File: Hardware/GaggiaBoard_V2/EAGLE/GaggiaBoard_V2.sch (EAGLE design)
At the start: 127 parts, among them IC1 LD117AS33TR, IC2 LD117AS33TR, J10 PIN262409-1, J11 PIN262409-1, J12 PIN262409-1, J13 PIN262409-1, J14 PIN262409-1, J15 PIN262409-1, J16 PIN262409-1, J17 PIN262409-1, J18 PIN262409-1, J19 PIN262409-1, J2 Vertical Qwiic Connector, J20 PIN262409-1, J21 PIN262409-1, J22 PIN262409-1, J23 PIN262409-1, J24 5033981892, J3 Vertical Qwiic Connector, J4 1X2-3.5MM, J5 1X2-3.5MM, K1 RELAY-SPDT-JZC-11F, K2 RELAY-SPDT-JZC-11F, K3 RELAY-SPDT-JZC-11F, Q1 600mA/40V, Q10 600mA/40V, Q11 MOSFET_PCH_DUAL-DMP2240UDM, Q2 600mA/40V, Q3 600mA/40V, Q4 600mA/40V, Q5 600mA/40V, Q6 600mA/40V, Q8 600mA/40V, Q9 600mA/40V, U1 BLACKPILL, U2 MAX31855K, U3 MAX31855K, U5 TXS0102

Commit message: V2 initial state
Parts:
- removed C14: 0.1uF, rcl:C-USC0603
- removed C4: 0.01uF, rcl:C-USC0603
- removed D6: (no value), adafruit:DIODESOD-123
- removed FB3, FB4: 470Ω, SparkFun-Coils:FERRITE_BEAD-0603-470Ω-100MHZ-1A-200MILIΩ
- removed J10, J21, J22, J23: PIN262409-1, con-faston:PIN262409-1
- removed LED4: (no value), adafruit:LEDCHIPLED_1206
- removed PSU2: IRM-10-5, discrete:IRM-10-5
- removed R29: 10K, rcl:R-US_R0603
- removed R30: 1K, rcl:R-US_R0603
- removed SPK1: SMT-0540-S-R, adafruit:SMT-0540-S-R
- removed U3: MAX31855K, SparkFun-IC-Conversion:MAX31855K
- added C15: 0.1uF, rcl:C-USC0603
- added H1: STANDOFF_ELECTRICAL, SparkFun-Hardware:STANDOFF_ELECTRICAL
- added SP1: SPEAKER/AL60P, adafruit:SPEAKER/AL60P
- F1: device special:FUSE2P -> special:FUSE
- J27: device SparkFun-Connectors:CONN_05NO_SILK -> SparkFun-Connectors:CONN_06NO_SILK_FEMALE_PTH
- J4: value 1X2-3.5MM -> (none); device adafruit:1X2-3.5MM -> SparkFun-Connectors:CONN_03SCREW; LCSC C474892 -> C474893
- J5: value 1X2-3.5MM -> 2PIN; device adafruit:1X2-3.5MM -> jst_eph:2PIN; LCSC C474892 -> C131337
- J6, J7, J9: value (none) -> 3PIN; device SparkFun-Connectors:CONN_03JST-PTH-VERT -> jst_eph:3PIN
- J8: value (none) -> 5PIN; device SparkFun-Connectors:CONN_05JST-VERT -> jst_eph:5PIN
- PSU1: value SM-PLG06-05 -> IRM-10-5; device discrete:SM-PLG06-05 -> discrete:IRM-10-5; SPICEPREFIX (none) -> E
- R12: value 51 -> 10K; LCSC C114628 -> C98220
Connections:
- net UART6_5V_RX renamed UART2_5V_RX
- net UART6_5V_TX renamed UART2_5V_TX
- removed net N$23: FB3.1, J5.1
- removed net N$25: C4.1, FB4.2, U3.T-
- removed net N$27: LED4.C, R12.2
- removed net N$31: C4.2, FB3.2, U3.T+
- removed net N$6: FB4.1, J5.2
- removed net PA2: J7.3, U1.PA2
- removed net PB2: J8.5, U1.PB2
- removed net RTS: C14.1, J27.5, R30.2
- removed net SPI2_MISO: U1.PB14, U2.(MI)SO, U3.(MI)SO
- removed net SPI2_NSS: U1.PB12, U2.!CS
- removed net SPI2_NSS2: U1.PB9, U3.!CS
- removed net SPI2_SCK: U1.PB13, U2.SCK, U3.SCK
- removed net UART6_RX: Q7G$2.S, R18.1, SJ2.1, U1.PA12
- removed net UART6_TX: Q7G$1.S, R19.1, SJ1.1, U1.PA11
- new net BOOT1: J27.6, U1.PB2
- new net PA15: R33.2, U1.PA15
- new net PB12: R6.1, U1.PB12
- new net PB13: R7.1, U1.PB13
- new net PB14: R28.1, U1.PB14
- new net PB15: J5.2, U1.PB15
- new net PB9: J8.5, U1.PB9
- new net UART2_RX: Q7G$2.S, R18.1, SJ2.1, U1.PA3
- new net UART2_TX: Q7G$1.S, R19.1, SJ1.1, U1.PA2
- net 3V3: now also C15.1; no longer C8.1, D1.C, D6.C, LED4.A, R27.2, R29.2, SPK1.-, U3.VCC
- net 3WAY: now also J16.1, K3.NO; no longer J11.1, K1.NO
- net 5V: now also C8.1, D1.C, R12.2, R27.2, SP1.-; no longer PSU2.VO+
- net AC_N: now also J15.1, J18.1, J19.1; no longer J10.1, J16.1, J21.1, J22.1, PSU2.AC_N
- net AC_P: now also F1.2, J13.1; no longer F1.2A, J15.1, J19.1, PSU2.AC_L
- net GND: now also C15.2, H1.P$1, J4.3, J5.1; no longer PSU2.VO-, R12.1, R30.1, U3.GND
- net HEATER_1: no longer J13.1
- net HEATER_2: now also J11.1, K1.NO; no longer J17.1, J18.1, K3.NO
- net I2C1_SCL: now also U5.A1
- net I2C1_SDA: now also U5.A2
- net I2C2_SCL: no longer U5.A1
- net I2C2_SDA: no longer U5.A2
- net N$1: now also F1.1, J20.1; no longer F1.1A, J23.1
- net N$3: now also J4.1; no longer J4.2
- net N$30: now also R12.1, SP1.+; no longer SPK1.+
- net N$4: now also J4.2; no longer J4.1
- net N$41: now also J9.3; no longer J9.2
- net N$42: now also J9.2; no longer J9.3
- net NRST: now also J27.5; no longer C14.2, D6.A, R29.1
- net PA1: now also R1.1; no longer J7.2
- net PA6: now also U2.!CS; no longer R34.2
- net PA8: now also R34.2; no longer R33.2
- net PB1: no longer J8.1
- net PB5: no longer R28.1
- net PB8: now also J8.1; no longer R1.1
- net PC14: now also J7.3; no longer R7.1
- net PC15: now also J7.2; no longer R6.1
- net PUMP_P: now also J17.1; no longer J20.1
- net SPI1_MISO: now also U2.(MI)SO
- net SPI1_SCK: now also U2.SCK
- net UART1_RX: now also J27.2; no longer J27.3
- net UART1_TX: now also J27.3; no longer J27.2
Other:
- moved on the sheet: C10, C11, C13, C3, C8, C9, D2, D3, D4, FB1, FB2, J11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

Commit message: part list fix
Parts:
- IC1, IC2: LCSC C152529 -> C26537
- LED1, LED2, LED3: LCSC C375534 -> C125086
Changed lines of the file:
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@@
 </part>
 <part name="LED1" library="adafruit" library_urn="urn:adsk.eagle:library:420" deviceset="LED" device="CHIPLED_1206" package3d_urn="urn:adsk.eagle:package:6240560/1" override_package3d_urn="urn:adsk.eagle:package:36462256/4" override_package_urn="urn:adsk.eagle:footprint:6239914/1">
-<attribute name="LCSC" value="C375534"/>
+<attribute name="LCSC" value="C125086"/>
 </part>
 <part name="LED2" library="adafruit" library_urn="urn:adsk.eagle:library:420" deviceset="LED" device="CHIPLED_1206" package3d_urn="urn:adsk.eagle:package:6240560/1" override_package3d_urn="urn:adsk.eagle:package:36462272/2" override_package_urn="urn:adsk.eagle:footprint:6239914/1">
-<attribute name="LCSC" value="C375534"/>
+<attribute name="LCSC" value="C125086"/>
 </part>
 <part name="LED3" library="adafruit" library_urn="urn:adsk.eagle:library:420" deviceset="LED" device="CHIPLED_1206" package3d_urn="urn:adsk.eagle:package:6240560/1" override_package3d_urn="urn:adsk.eagle:package:36462279/2" override_package_urn="urn:adsk.eagle:footprint:6239914/1">
-<attribute name="LCSC" value="C375534"/>
+<attribute name="LCSC" value="C125086"/>
 </part>
 <part name="R10" library="rcl" library_urn="urn:adsk.eagle:library:334" deviceset="R-US_" device="R0603" package3d_urn="urn:adsk.eagle:package:23555/3" value="120">
@@
 </part>
 <part name="IC1" library="v-reg" library_urn="urn:adsk.eagle:library:409" deviceset="LD117A?*" device="S" package3d_urn="urn:adsk.eagle:package:30370/1" override_package3d_urn="urn:adsk.eagle:package:36461295/2" override_package_urn="urn:adsk.eagle:footprint:30315/1" technology="33TR" value="LD117AS33TR">
-<attribute name="LCSC" value="C152529"/>
+<attribute name="LCSC" value="C26537"/>
 </part>
 <part name="SUPPLY9" library="Power_Symbols" library_urn="urn:adsk.eagle:library:16502351" deviceset="GND-BAR" device="" value="GND"/>
@@
 </part>
 <part name="IC2" library="v-reg" library_urn="urn:adsk.eagle:library:409" deviceset="LD117A?*" device="S" package3d_urn="urn:adsk.eagle:package:30370/1" override_package3d_urn="urn:adsk.eagle:package:36461293/2" override_package_urn="urn:adsk.eagle:footprint:30315/1" technology="33TR" value="LD117AS33TR">
-<attribute name="LCSC" value="C152529"/>
+<attribute name="LCSC" value="C26537"/>
 </part>
 <part name="SUPPLY13" library="Power_Symbols" library_urn="urn:adsk.eagle:library:16502351" deviceset="GND-BAR" device="" value="GND"/>

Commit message: V2.1 update
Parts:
- removed IC2: LD117AS33TR, v-reg:LD117AS33TR
- removed J24: 5033981892, discrete:5033981892
- removed Q7: (no value), microbuilder:MOSFET-N_DUAL
- removed R16, R17, R18, R19: 10K, rcl:R-US_R0603
- removed SJ1, SJ2: (no value), microbuilder:SOLDERJUMPER
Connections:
- removed net UART2_5V_RX: J1.2, Q7G$2.D, R16.1, SJ2.2
- removed net UART2_5V_TX: J1.3, Q7G$1.D, R17.1, SJ1.2
- net 3V3: no longer IC2.OUT, J24.VDD, Q7G$1.G, Q7G$2.G, R18.2, R19.2
- net 5V: no longer IC2.IN, R16.2, R17.2
- net GND: no longer IC2.ADJ, J24.VSS
- net SPI1_MISO: no longer J24.DAT0
- net SPI1_MOSI: no longer J24.CMD
- net SPI1_NSS: no longer J24.CD/DAT3
- net SPI1_SCK: no longer J24.CLK
- net UART2_RX: now also J1.2; no longer Q7G$2.S, R18.1, SJ2.1
- net UART2_TX: now also J1.3; no longer Q7G$1.S, R19.1, SJ1.1
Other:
- moved on the sheet: IC1

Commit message: J1 fix
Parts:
- J1: value (none) -> 4PIN; device SparkFun-Connectors:CONN_04POLAR -> jst_exh:4PIN
- PSU1: LCSC (none) -> C2857903
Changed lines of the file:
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@@
 </classes>
 <parts>
-<part name="J1" library="SparkFun-Connectors" deviceset="CONN_04" device="POLAR" override_package3d_urn="urn:adsk.eagle:package:36462044/3" override_package_urn="urn:adsk.eagle:footprint:36462045/1">
-<attribute name="LCSC" value="C144395"/>
-</part>
 <part name="U1" library="discrete" library_urn="urn:adsk.eagle:library:211" deviceset="BLACKPILL" device="" override_package3d_urn="urn:adsk.eagle:package:36462313/2" override_package_urn="urn:adsk.eagle:footprint:36462314/1"/>
 <part name="J2" library="SparkFun-Connectors" deviceset="QWIIC_CONNECTOR" device="" override_package3d_urn="urn:adsk.eagle:package:36462029/2" override_package_urn="urn:adsk.eagle:footprint:36462030/1" value="Vertical Qwiic Connector">
@@
 </part>
 <part name="PSU1" library="discrete" deviceset="IRM-10-5" device="" override_package3d_urn="urn:adsk.eagle:package:36415007/2" override_package_urn="urn:adsk.eagle:footprint:36415008/1" override_locally_modified="yes">
+<attribute name="LCSC" value="C2857903"/>
 <attribute name="SPICEPREFIX" value="E"/>
 </part>
@@
 </spice>
 <attribute name="LCSC" value="C98220"/>
+</part>
+<part name="J1" library="jst_exh" deviceset="4PIN" device="" override_package3d_urn="urn:adsk.eagle:package:37572770/2" override_package_urn="urn:adsk.eagle:footprint:37572771/1">
+<attribute name="LCSC" value="C144395"/>
 </part>
 </parts>
@@
 </plain>
 <instances>
-<instance part="J1" gate="J1" x="10.16" y="170.18" smashed="yes">
-<attribute name="VALUE" x="5.08" y="162.814" size="1.778" layer="96" font="vector"/>
-<attribute name="NAME" x="5.08" y="178.308" size="1.778" layer="95" font="vector"/>
-<attribute name="LCSC" x="10.16" y="170.18" size="1.778" layer="96" display="off"/>
-</instance>
 <instance part="U1" gate="G$1" x="203.2" y="144.78" smashed="yes">
 <attribute name="NAME" x="193.04" y="173.482" size="1.27" layer="94"/>
@@
 <attribute name="VALUE" x="55.88" y="165.735" size="1.778" layer="96" align="center"/>
 </instance>
+<instance part="J1" gate="G$1" x="12.7" y="170.18" smashed="yes" rot="R180">
+<attribute name="NAME" x="12.7" y="180.34" size="1.27" layer="95" rot="R180"/>
+<attribute name="LCSC" x="12.7" y="170.18" size="1.778" layer="96" rot="R180" display="off"/>
+</instance>
 </instances>
 <busses>
@@
 <net name="GND" class="0">
 <segment>
-<pinref part="J1" gate="J1" pin="4"/>
-<wire x1="15.24" y1="175.26" x2="22.86" y2="175.26" width="0.1524" layer="91"/>
-<label x="17.78" y="175.26" size="1.778" layer="95"/>
+<label x="20.32" y="175.26" size="1.778" layer="95"/>
+<wire x1="17.78" y1="175.26" x2="27.94" y2="175.26" width="0.1524" layer="91"/>
+<pinref part="J1" gate="G$1" pin="4"/>
 </segment>
 <segment>
@@
 <net name="5V" class="0">
 <segment>
-<pinref part="J1" gate="J1" pin="1"/>
-<wire x1="15.24" y1="167.64" x2="22.86" y2="167.64" width="0.1524" layer="91"/>
 <label x="20.32" y="167.64" size="1.778" layer="95"/>
+<wire x1="17.78" y1="167.64" x2="27.94" y2="167.64" width="0.1524" layer="91"/>
+<pinref part="J1" gate="G$1" pin="1"/>
 </segment>
 <segment>
@@
 </segment>
 <segment>
-<pinref part="J1" gate="J1" pin="2"/>
-<wire x1="15.24" y1="170.18" x2="22.86" y2="170.18" width="0.1524" layer="91"/>
-<label x="17.78" y="170.18" size="1.778" layer="95"/>
+<label x="20.32" y="170.18" size="1.778" layer="95"/>
+<wire x1="17.78" y1="170.18" x2="27.94" y2="170.18" width="0.1524" layer="91"/>
+<pinref part="J1" gate="G$1" pin="2"/>
 </segment>
 </net>
@@
 </segment>
 <segment>
-<pinref part="J1" gate="J1" pin="3"/>
-<wire x1="15.24" y1="172.72" x2="22.86" y2="172.72" width="0.1524" layer="91"/>
-<label x="17.78" y="172.72" size="1.778" layer="95"/>
+<label x="20.32" y="172.72" size="1.778" layer="95"/>
+<wire x1="17.78" y1="172.72" x2="27.94" y2="172.72" width="0.1524" layer="91"/>
+<pinref part="J1" gate="G$1" pin="3"/>
 </segment>
 </net>
@@
 <attribute name="NAME" x="55.88" y="43.18" size="1.27" layer="95"/>
 <attribute name="VALUE" x="55.88" y="27.94" size="1.27" layer="96"/>
+<attribute name="LCSC" x="63.5" y="35.56" size="1.778" layer="96" display="off"/>
 </instance>
 <instance part="SUPPLY23" gate="G$1" x="78.74" y="27.94" smashed="yes">

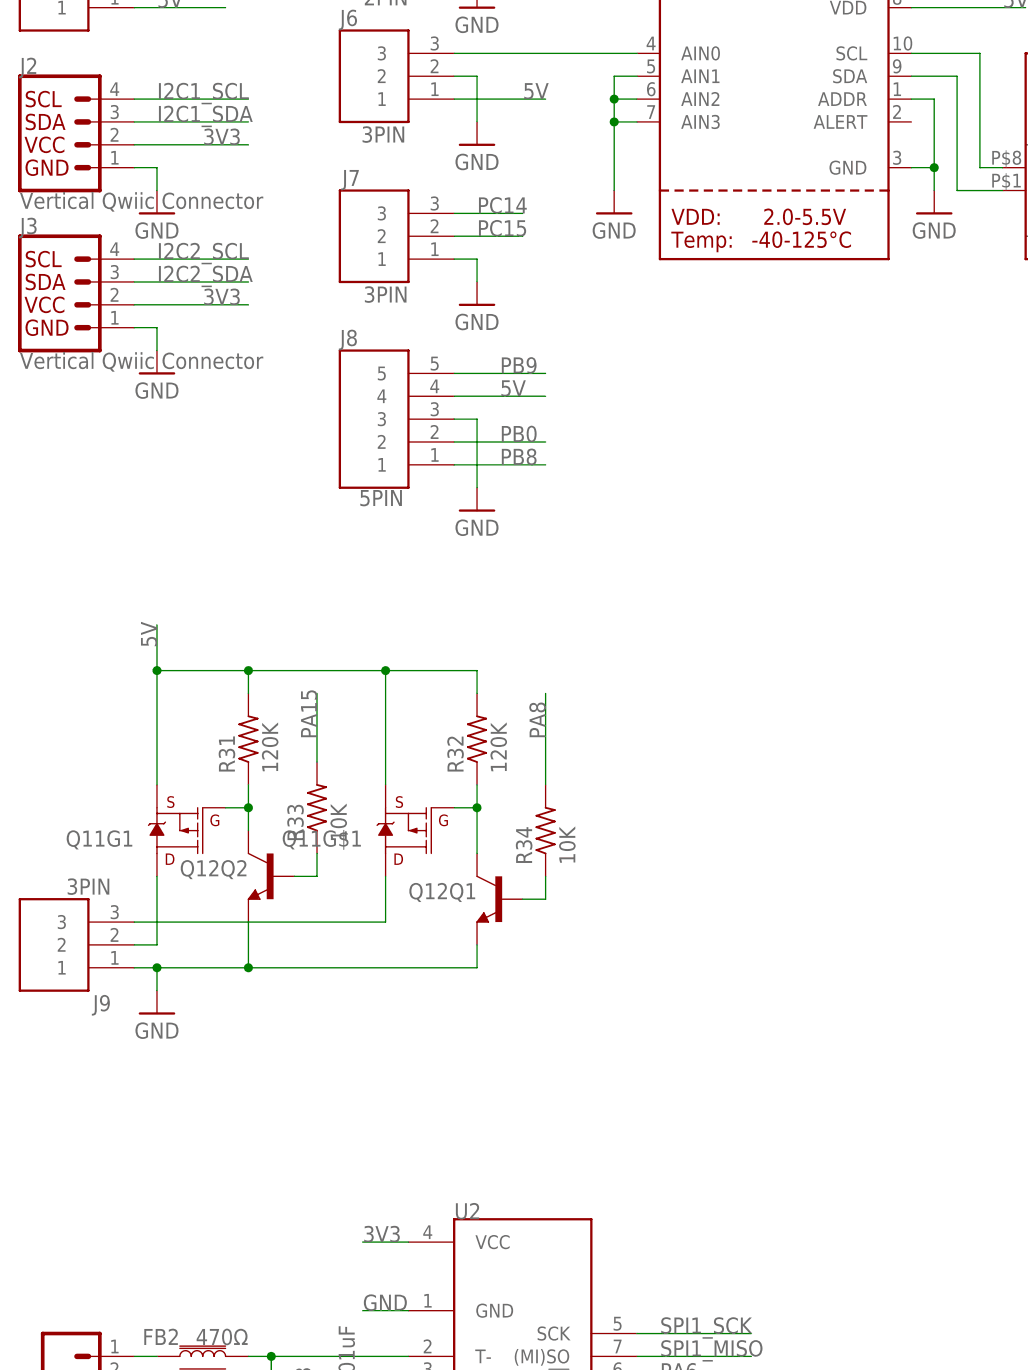
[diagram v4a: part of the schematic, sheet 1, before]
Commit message: 3-Way valve SSR
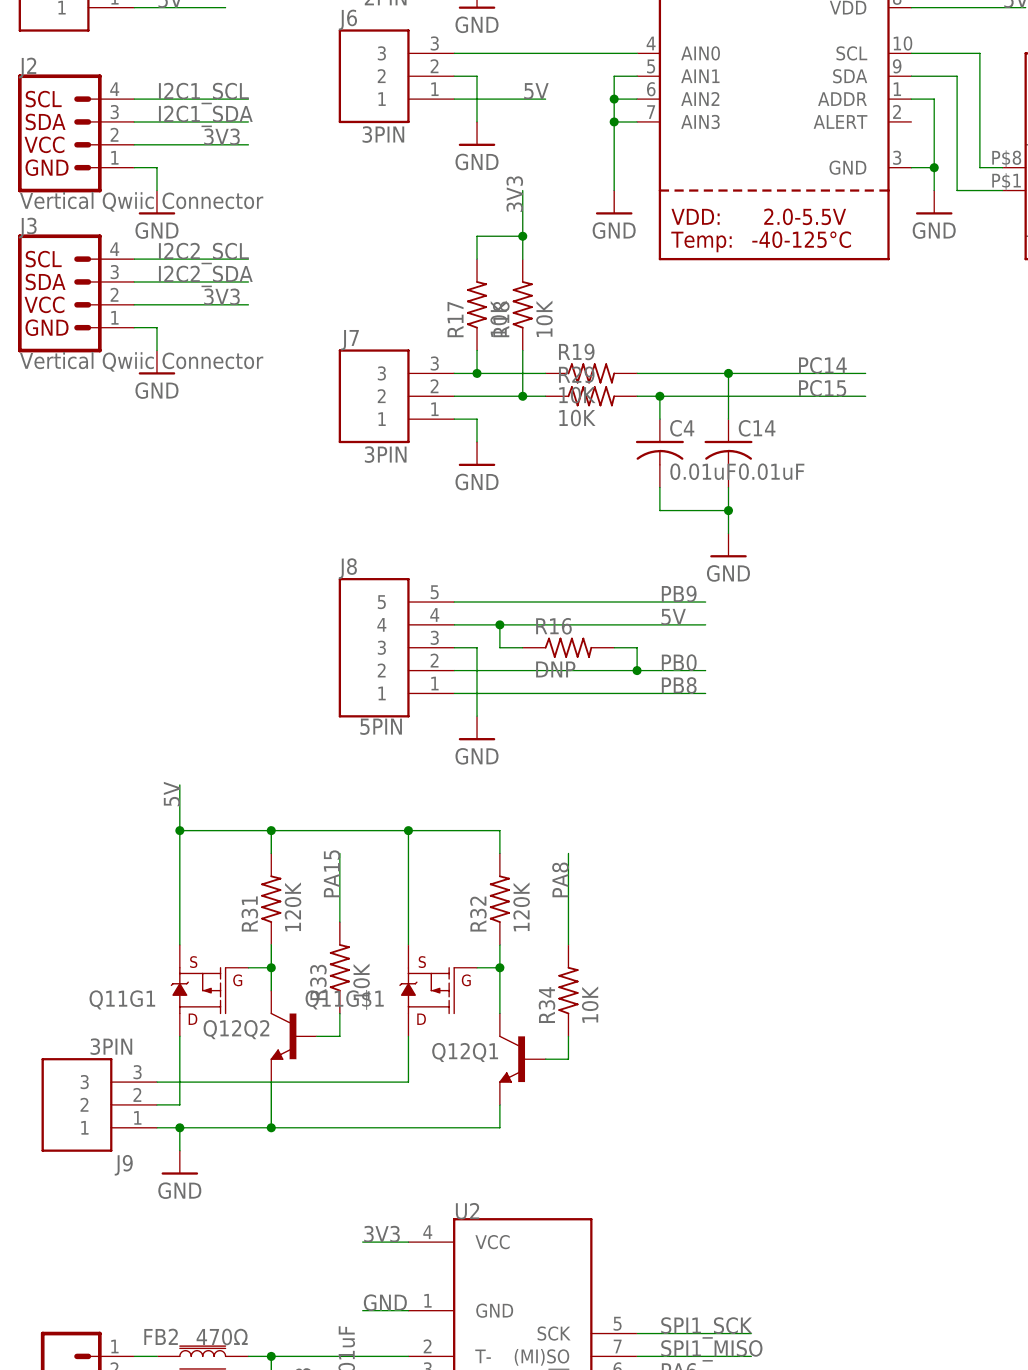
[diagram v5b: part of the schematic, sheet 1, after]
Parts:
- removed D4: S1M, diode:S1M
- added C14, C4: 0.01uF, rcl:C-USC0603
- added R16: DNP, rcl:R-US_R0603
- added R17, R18, R19, R29: 10K, rcl:R-US_R0603
- added R30: 220, rcl:R-US_R0603
- K3: value RELAY-SPDT-JZC-11F -> AQH213; device SparkFun-Electromechanical:RELAY-SPDT-JZC-11F -> relay:AQH213; LCSC C74541 -> C719560
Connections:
- new net N$23: J7.2, R18.1, R29.1
- new net N$25: K3.A, R30.2
- new net N$6: J7.3, R17.1, R19.1
- net 3V3: now also R17.2, R18.2
- net 3WAY: now also K3.DS1; no longer K3.NO
- net 5V: now also R16.1, R30.1; no longer D4.C, K3.COIL1
- net AC_P: now also K3.DS3; no longer K3.MAIN, K3.NC
- net GND: now also C14.2, C4.2
- net N$12: now also K3.K, K3.K1, K3.K2; no longer D4.A, K3.COIL2
- net PB0: now also R16.2
- net PC14: now also C14.1, R19.2; no longer J7.3
- net PC15: now also C4.1, R29.2; no longer J7.2
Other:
- moved on the sheet: J16, J7, J8, J9, Q11G$1, Q11G1, Q12Q1, Q12Q2, R31, R32, R33, R34
